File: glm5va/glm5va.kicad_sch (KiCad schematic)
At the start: 21 parts, among them J1 Conn_02x10_Odd_Even, J2 JIN, J3 POWER, U1 74HC245, U2 74HC245

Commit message: GbSwitchFp
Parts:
- C1, C2: value C -> 100n
- J1: value Conn_02x10_Odd_Even -> BANK_xx1
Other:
- moved on the sheet: R4
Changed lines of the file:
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@@
 	(wire
 		(pts
-			(xy 224.79 82.55) (xy 233.68 82.55)
+			(xy 224.79 82.55) (xy 227.33 82.55)
 		)
 		(stroke
@@
 	(wire
 		(pts
-			(xy 241.3 82.55) (xy 243.84 82.55)
+			(xy 234.95 82.55) (xy 238.76 82.55)
 		)
 		(stroke
@@
 		(dnp no)
 		(property "Reference" "C1"
-			(at 81.28 40.64 90)
+			(at 81.534 43.688 90)
 			(effects
 				(font
@@
 			)
 		)
-		(property "Value" "C"
-			(at 81.28 43.18 90)
+		(property "Value" "100n"
+			(at 80.772 53.086 90)
 			(effects
 				(font
@@
 	(symbol
 		(lib_id "Device:R")
-		(at 237.49 82.55 90)
+		(at 231.14 82.55 90)
 		(unit 1)
 		(exclude_from_sim no)
@@
 		(dnp no)
 		(property "Reference" "R4"
-			(at 237.236 80.01 90)
+			(at 230.886 80.01 90)
 			(effects
 				(font
@@
 		)
 		(property "Value" "0"
-			(at 237.236 85.344 90)
+			(at 230.886 85.344 90)
 			(effects
 				(font
@@
 		)
 		(property "Footprint" ""
-			(at 237.49 84.328 90)
+			(at 231.14 84.328 90)
 			(effects
 				(font
@@
 		)
 		(property "Datasheet" "~"
-			(at 237.49 82.55 0)
+			(at 231.14 82.55 0)
 			(effects
 				(font
@@
 		)
 		(property "Description" "Resistor"
-			(at 237.49 82.55 0)
+			(at 231.14 82.55 0)
 			(effects
 				(font
@@
 	(symbol
 		(lib_id "power:+5V")
-		(at 243.84 82.55 270)
+		(at 238.76 82.55 270)
 		(mirror x)
 		(unit 1)
@@
 		(fields_autoplaced yes)
 		(property "Reference" "#PWR015"
-			(at 240.03 82.55 0)
+			(at 234.95 82.55 0)
 			(effects
 				(font
@@
 		)
 		(property "Value" "+5V"
-			(at 247.65 82.5499 90)
+			(at 242.57 82.5499 90)
 			(effects
 				(font
@@
 		)
 		(property "Footprint" ""
-			(at 243.84 82.55 0)
+			(at 238.76 82.55 0)
 			(effects
 				(font
@@
 		)
 		(property "Datasheet" ""
-			(at 243.84 82.55 0)
+			(at 238.76 82.55 0)
 			(effects
 				(font
@@
 		)
 		(property "Description" "Power symbol creates a global label with name \"+5V\""
-			(at 243.84 82.55 0)
+			(at 238.76 82.55 0)
 			(effects
 				(font
@@
 			)
 		)
-		(property "Value" "C"
+		(property "Value" "100n"
 			(at 232.41 52.07 90)
 			(effects
@@
 			)
 		)
-		(property "Value" "Conn_02x10_Odd_Even"
+		(property "Value" "BANK_xx1"
 			(at 147.32 111.76 0)
 			(effects

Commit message: glm5va: footprint association
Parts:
- C1, C2: footprint (none) -> Capacitor_SMD:C_0603_1608Metric
- FPGA_LED1, FPGA_LED2, FPGA_LED4, LED3: footprint OLIMEX_LEDs-FP:LED_0603_KA -> LED_SMD:LED_1206_3216Metric
- J1: footprint (none) -> Connector_PinHeader_2.54mm:PinHeader_2x10_P2.54mm_Vertical
- J2: footprint (none) -> Connector_IDC:IDC-Header_2x08_P2.54mm_Vertical
- J3: footprint (none) -> Connector_Molex:Molex_KK-396_A-41791-0004_1x04_P3.96mm_Vertical
- R1, R2, R3, R4: footprint (none) -> Resistor_SMD:R_0603_1608Metric
- R5, R6, R7, R8: footprint OLIMEX_RLC-FP:R_0402_5MIL_DWS -> Resistor_SMD:R_0603_1608Metric
- TP1, TP2: footprint (none) -> Connector_Pin:Pin_D1.0mm_L10.0mm
- U1, U2: footprint (none) -> Package_SO:TSSOP-20_4.4x6.5mm_P0.65mm
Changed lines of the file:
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@@
 			)
 		)
-		(property "Footprint" "OLIMEX_LEDs-FP:LED_0603_KA"
+		(property "Footprint" "LED_SMD:LED_1206_3216Metric"
 			(at 185.42 30.48 0)
 			(effects
@@
 			)
 		)
-		(property "Footprint" ""
+		(property "Footprint" "Capacitor_SMD:C_0603_1608Metric"
 			(at 85.09 47.2948 0)
 			(effects
@@
 			)
 		)
-		(property "Footprint" ""
+		(property "Footprint" "Resistor_SMD:R_0603_1608Metric"
 			(at 231.14 84.328 90)
 			(effects
@@
 			)
 		)
-		(property "Footprint" "OLIMEX_LEDs-FP:LED_0603_KA"
+		(property "Footprint" "LED_SMD:LED_1206_3216Metric"
 			(at 165.1 30.48 0)
 			(effects
@@
 			)
 		)
-		(property "Footprint" ""
+		(property "Footprint" "Connector_IDC:IDC-Header_2x08_P2.54mm_Vertical"
 			(at 139.7 67.31 0)
 			(effects
@@
 			)
 		)
-		(property "Footprint" ""
+		(property "Footprint" "Connector_Molex:Molex_KK-396_A-41791-0004_1x04_P3.96mm_Vertical"
 			(at 246.38 26.67 0)
 			(effects
@@
 			)
 		)
-		(property "Footprint" "OLIMEX_RLC-FP:R_0402_5MIL_DWS"
+		(property "Footprint" "Resistor_SMD:R_0603_1608Metric"
 			(at 173.482 46.99 0)
 			(effects
@@
 			)
 		)
-		(property "Footprint" ""
+		(property "Footprint" "Resistor_SMD:R_0603_1608Metric"
 			(at 87.122 90.17 90)
 			(effects
@@
 			)
 		)
-		(property "Footprint" "OLIMEX_LEDs-FP:LED_0603_KA"
+		(property "Footprint" "LED_SMD:LED_1206_3216Metric"
 			(at 175.26 30.48 0)
 			(effects
@@
 			)
 		)
-		(property "Footprint" ""
+		(property "Footprint" "Connector_Pin:Pin_D1.0mm_L10.0mm"
 			(at 121.92 109.22 0)
 			(effects
@@
 			)
 		)
-		(property "Footprint" "OLIMEX_RLC-FP:R_0402_5MIL_DWS"
+		(property "Footprint" "Resistor_SMD:R_0603_1608Metric"
 			(at 183.642 46.99 0)
 			(effects
@@
 			)
 		)
-		(property "Footprint" ""
+		(property "Footprint" "Capacitor_SMD:C_0603_1608Metric"
 			(at 228.6 47.9552 0)
 			(effects
@@
 			)
 		)
-		(property "Footprint" ""
+		(property "Footprint" "Package_SO:TSSOP-20_4.4x6.5mm_P0.65mm"
 			(at 104.14 72.39 0)
 			(effects
@@
 			)
 		)
-		(property "Footprint" "OLIMEX_LEDs-FP:LED_0603_KA"
+		(property "Footprint" "LED_SMD:LED_1206_3216Metric"
 			(at 195.58 30.48 0)
 			(effects
@@
 			)
 		)
-		(property "Footprint" ""
+		(property "Footprint" "Connector_PinHeader_2.54mm:PinHeader_2x10_P2.54mm_Vertical"
 			(at 146.05 125.73 0)
 			(effects
@@
 			)
 		)
-		(property "Footprint" ""
+		(property "Footprint" "Connector_Pin:Pin_D1.0mm_L10.0mm"
 			(at 135.89 109.22 0)
 			(effects
@@
 			)
 		)
-		(property "Footprint" ""
+		(property "Footprint" "Resistor_SMD:R_0603_1608Metric"
 			(at 82.55 84.328 90)
 			(effects
@@
 			)
 		)
-		(property "Footprint" "OLIMEX_RLC-FP:R_0402_5MIL_DWS"
+		(property "Footprint" "Resistor_SMD:R_0603_1608Metric"
 			(at 193.802 46.99 0)
 			(effects
@@
 			)
 		)
-		(property "Footprint" "OLIMEX_RLC-FP:R_0402_5MIL_DWS"
+		(property "Footprint" "Resistor_SMD:R_0603_1608Metric"
 			(at 163.322 46.99 0)
 			(effects
@@
 			)
 		)
-		(property "Footprint" ""
+		(property "Footprint" "Resistor_SMD:R_0603_1608Metric"
 			(at 223.012 90.17 90)
 			(effects
@@
 			)
 		)
-		(property "Footprint" ""
+		(property "Footprint" "Package_SO:TSSOP-20_4.4x6.5mm_P0.65mm"
 			(at 212.09 72.39 0)
 			(effects

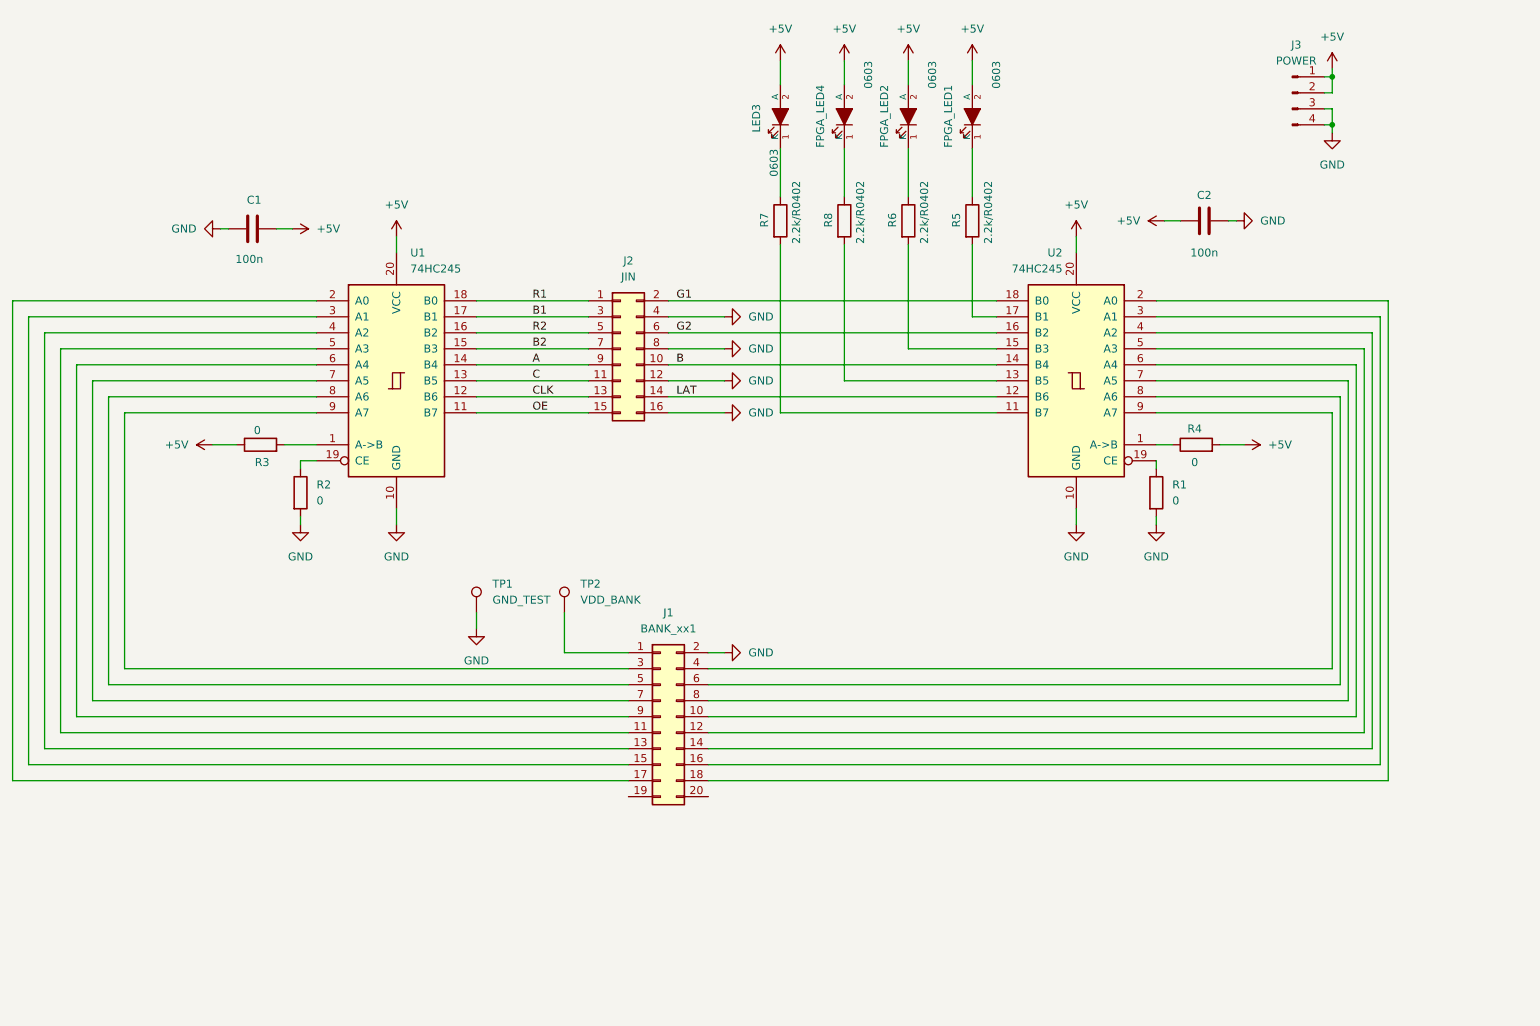
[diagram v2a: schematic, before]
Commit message: glm5va: place components
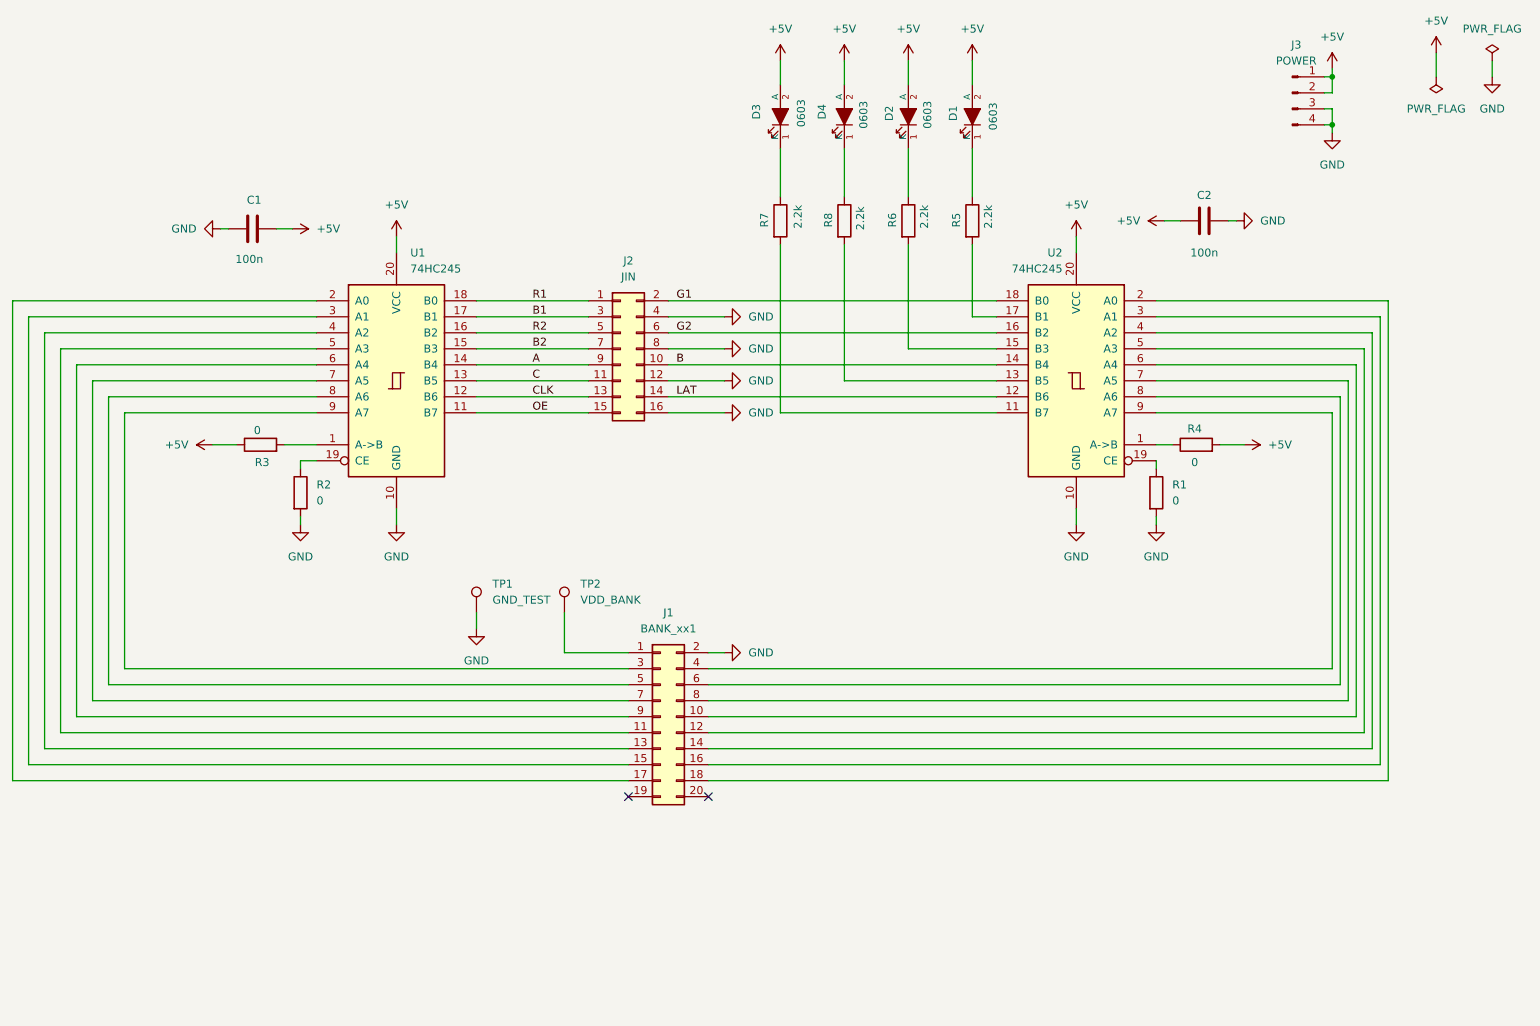
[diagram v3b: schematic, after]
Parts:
- R5, R6, R7, R8: value 2.2k/R0402 -> 2.2k
- renumbered FPGA_LED1 to D1, FPGA_LED2 to D2, LED3 to D3, FPGA_LED4 to D4
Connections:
- no-connect marks 0 -> 2

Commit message: glm5va: routing and layers ok
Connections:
- net +5V: now also J3.3 (Pin_3), J3.4 (Pin_4); no longer J3.1 (Pin_1), J3.2 (Pin_2)
- net GND: now also J3.1 (Pin_1), J3.2 (Pin_2); no longer J3.3 (Pin_3), J3.4 (Pin_4)
- net BANK_A1: now reaches J1.17 (Pin_17)
- net BANK_A1: now also U2.8 (A6); no longer U1.2 (A0)
- net BANK_A2: now reaches J1.15 (Pin_15)
- net BANK_A2: now also U2.6 (A4); no longer U1.3 (A1)
- net BANK_A3: now reaches J1.13 (Pin_13)
- net BANK_A3: now also U2.4 (A2); no longer U1.4 (A2)
- net BANK_A4: now reaches J1.11 (Pin_11)
- net BANK_A4: now also U2.2 (A0); no longer U1.5 (A3)
- net BANK_A5: now reaches J1.9 (Pin_9)
- net BANK_A5: now also U1.8 (A6); no longer U1.6 (A4)
- net BANK_A6: now reaches J1.7 (Pin_7)
- net BANK_A6: now also U1.6 (A4); no longer U1.7 (A5)
- net BANK_A7: now reaches J1.5 (Pin_5)
- net BANK_A7: now also U1.4 (A2); no longer U1.8 (A6)
- net BANK_A8: now reaches J1.3 (Pin_3)
- net BANK_A8: now also U1.2 (A0); no longer U1.9 (A7)
- net BANK_B5: now reaches J1.10 (Pin_10)
- net BANK_B5: now also U1.9 (A7); no longer U2.6 (A4)
- net BANK_B3: now reaches U2.5 (A3)
- net BANK_B3: now also J1.14 (Pin_14); no longer J1.12 (Pin_12)
- net BANK_B2: now reaches J1.16 (Pin_16)
- net BANK_B2: now also U2.7 (A5); no longer U2.3 (A1)
- net BANK_B1: now reaches J1.18 (Pin_18)
- net BANK_B1: now also U2.9 (A7); no longer U2.2 (A0)
- net BANK_B8: now reaches J1.4 (Pin_4)
- net BANK_B8: now also U1.3 (A1); no longer U2.9 (A7)
- net BANK_B7: now reaches J1.6 (Pin_6)
- net BANK_B7: now also U1.5 (A3); no longer U2.8 (A6)
- net BANK_B6: now reaches J1.8 (Pin_8)
- net BANK_B6: now also U1.7 (A5); no longer U2.7 (A5)
- new net BANK_B4: J1.12 (Pin_12), U2.3 (A1)
- no-connect marks 2 -> 3
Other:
- moved on the sheet: C1, C2, D1, D2, D3, D4, J1, J2, J3, R1, R2, R3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
